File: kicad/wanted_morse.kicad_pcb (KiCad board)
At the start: 2 copper layers, 41.9 x 49.5 mm, 5 parts, among them M2 MountingHole_2.2mm_M2

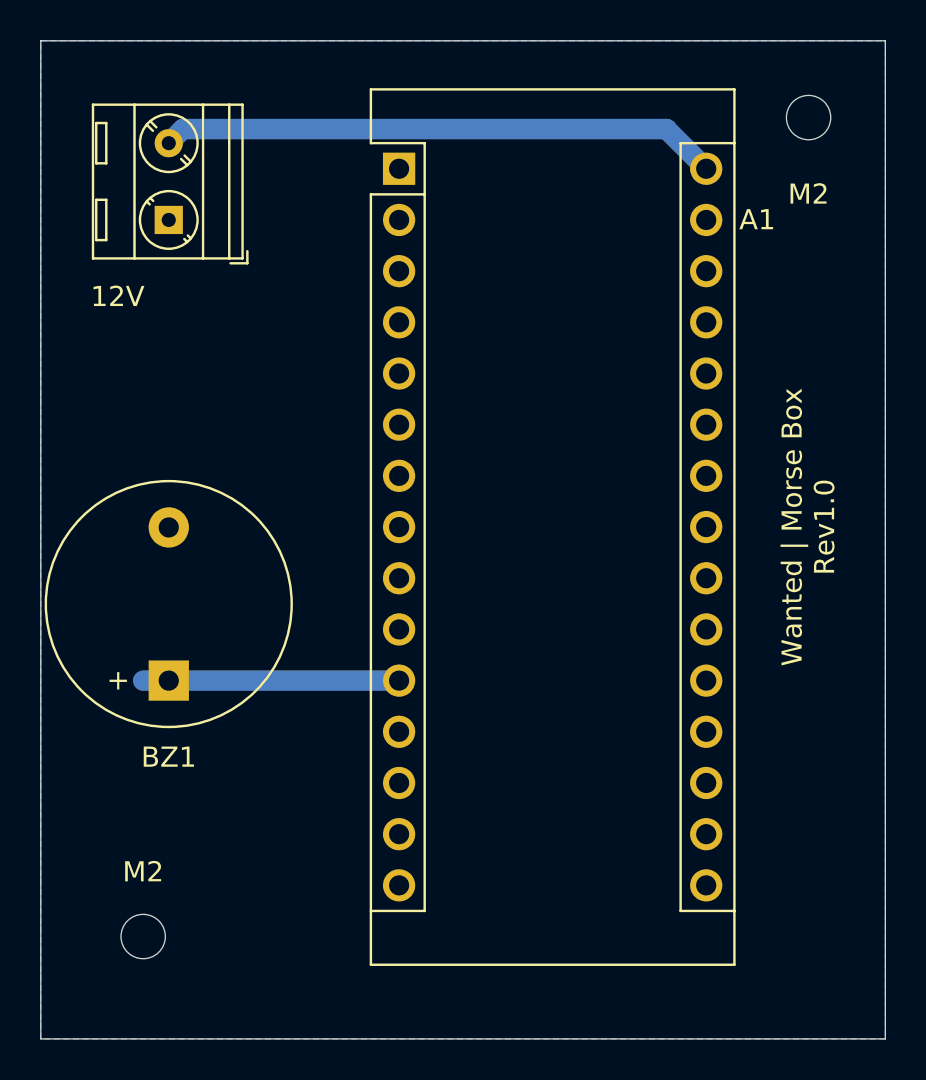
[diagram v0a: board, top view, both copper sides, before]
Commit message: added 3d printable mount
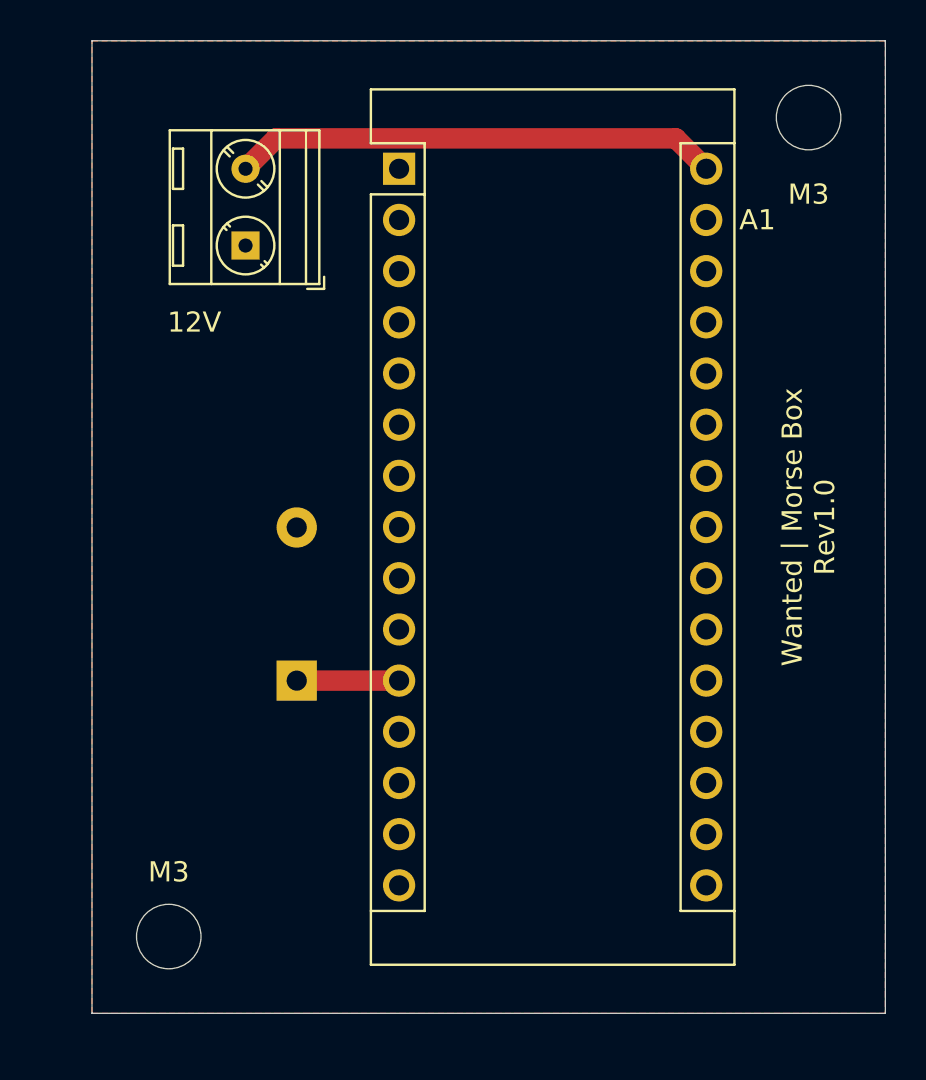
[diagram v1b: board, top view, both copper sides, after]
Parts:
- BZ1: moved to B.Cu
- moved BZ1 6.35 mm to (133.3, 71.1)
- moved 12V 4.02 mm to (130.8, 49.5)
- moved M3 1.27 mm to (127.0, 83.8)
- renumbered M2 to M3
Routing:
- net Net-(A1-Pad11): track 12.7 -> 5.08 mm
- net +12V: track 27.8 -> 24.1 mm
- added copper zone on F.Cu, net GND
- removed copper zone on B.Cu, net GND
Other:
- board size 41.9 x 49.5 mm -> 39.4 x 48.3 mm
